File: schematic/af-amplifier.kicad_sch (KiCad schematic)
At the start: 34 parts, among them J2 AudioJack3, Q5 2N3904, U7 TDA2003, U8 ADE-1L

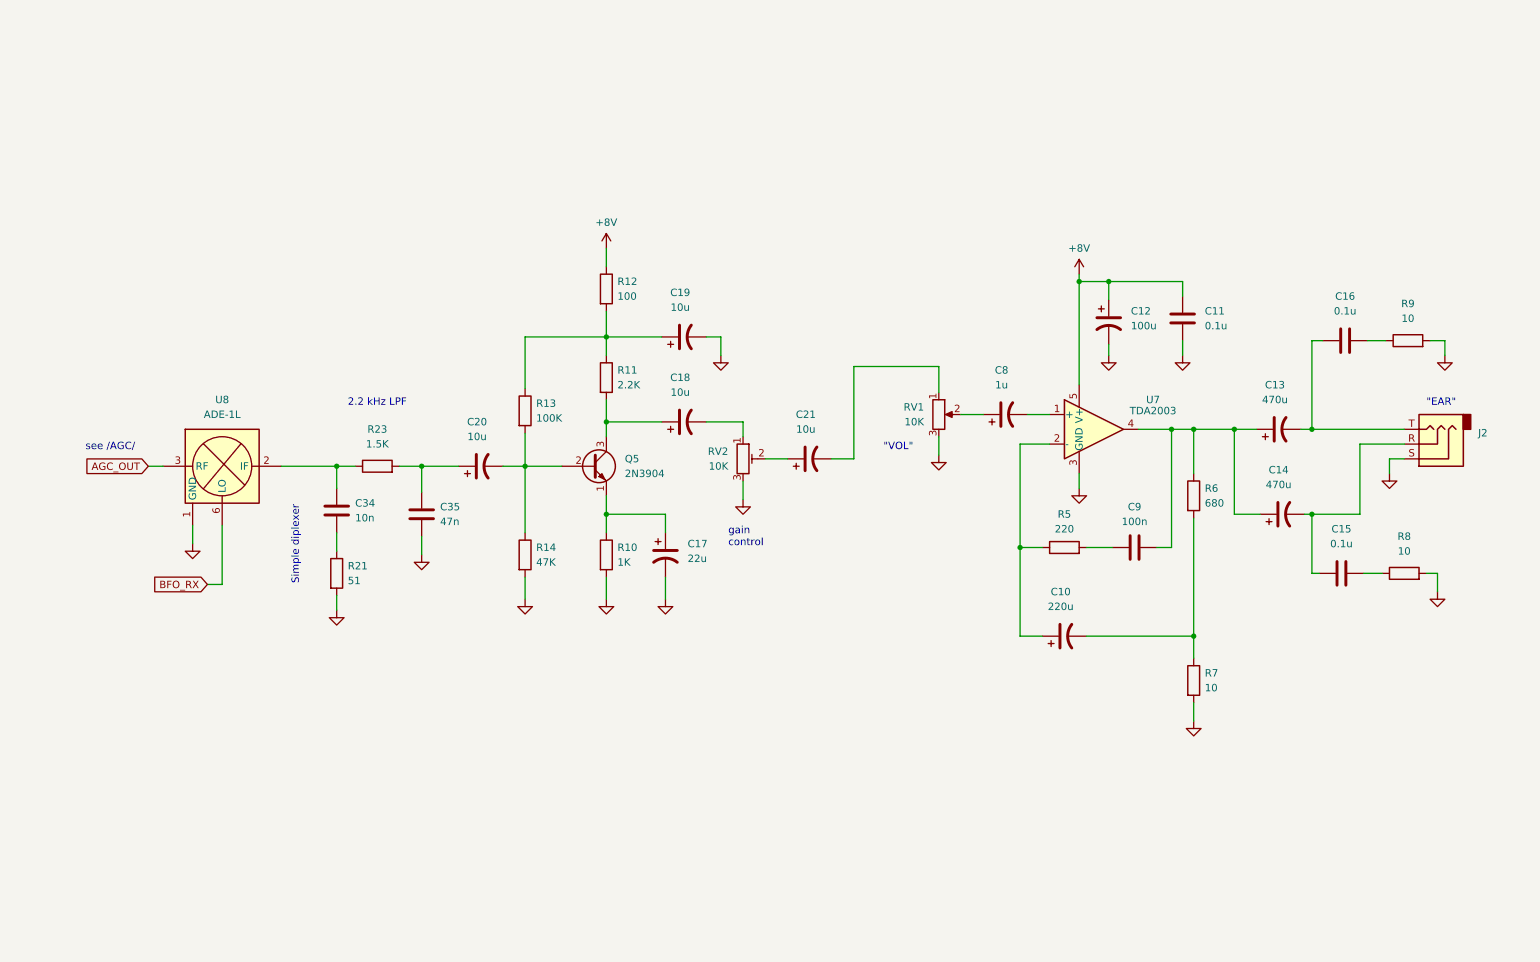
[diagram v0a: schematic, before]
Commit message: Schematic: add S-meter
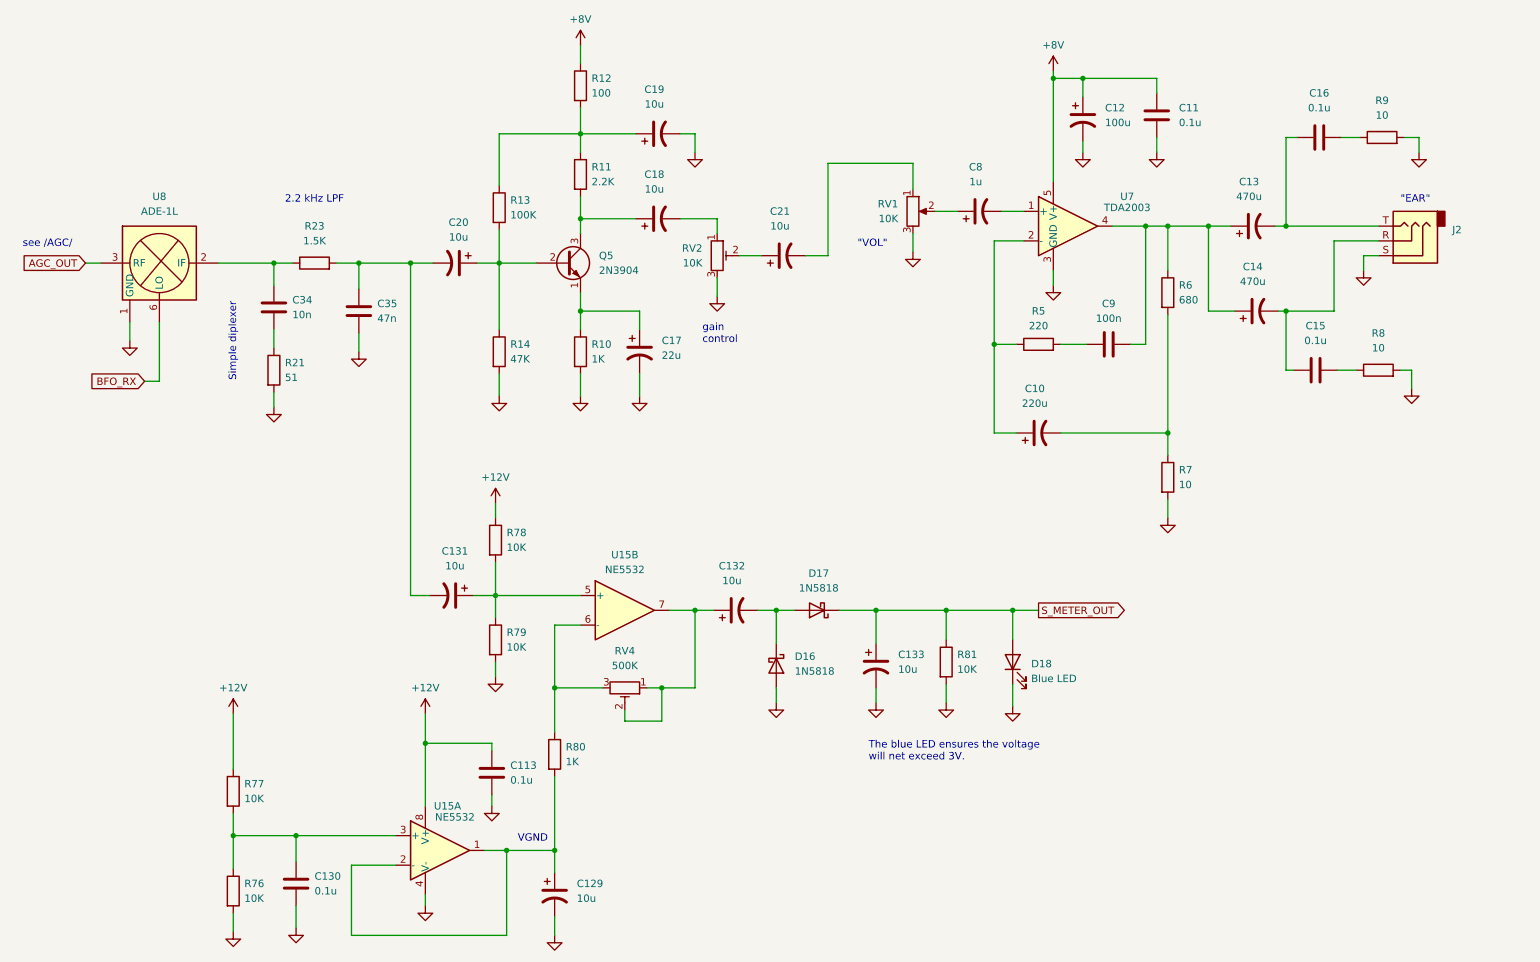
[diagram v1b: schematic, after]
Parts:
- added C113, C130: 0.1u, symbol Device:C
- added C129, C131, C132, C133: 10u, symbol Device:C_Polarized_US
- added D16, D17: 1N5818, Diode_THT:D_DO-41_SOD81_P10.16mm_Horizontal, symbol Diode:1N5818
- added D18: Blue LED, symbol Device:LED
- added R76, R77, R78, R79, R81: 10K, symbol Device:R
- added R80: 1K, symbol Device:R
- added RV4: 500K, symbol Device:R_Potentiometer_Trim
- added U15: NE5532, symbol Amplifier_Operational:NE5532
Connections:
- net GND: now also C113.2, C129.2, C130.2, C133.2, D16.2 (A), D18.1 (K), R76.2, R79.2, R81.2, U15.4 (V-)
- net at Q5.2 (B), R13.2, R14.1: now also C20.1; no longer C20.2
- net at C35.1, R23.2: now also C20.2, C131.2; no longer C20.1
- new net: C131.1, R78.2, R79.1, U15.5 (+)
- new net: C129.1, R80.2, U15.1, U15.2 (-)
- new net: C130.1, R76.1, R77.2, U15.3 (+)
- new net: C132.1, RV4.1, RV4.2, U15.7
- new net: C132.2, D16.1 (K), D17.2 (A)
- new net: R80.1, RV4.3, U15.6 (-)
- new net +12V: C113.1, R77.1, R78.1, U15.8 (V+)
- new net S_METER_OUT: C133.1, D17.1 (K), D18.2 (A), R81.1
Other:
- note added: "The blue LED ensures the voltage will net exceed 3V."
- note added: "VGND"
- moved on the sheet: C10, C11, C12, C13, C14, C15, C16, C17, C18, C19, C20, C21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

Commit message: Fix typo
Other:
- note added: "The blue LED ensures the voltage will not exceed 3V."
- note removed: "The blue LED ensures the voltage will net exceed 3V."
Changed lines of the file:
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@@
     (effects (font (size 1.27 1.27)) (justify left bottom))
   )
-  (text "The blue LED ensures the voltage\nwill net exceed 3V."
+  (text "The blue LED ensures the voltage\nwill not exceed 3V."
     (at 161.29 153.67 0)
     (effects (font (size 1.27 1.27)) (justify left bottom))

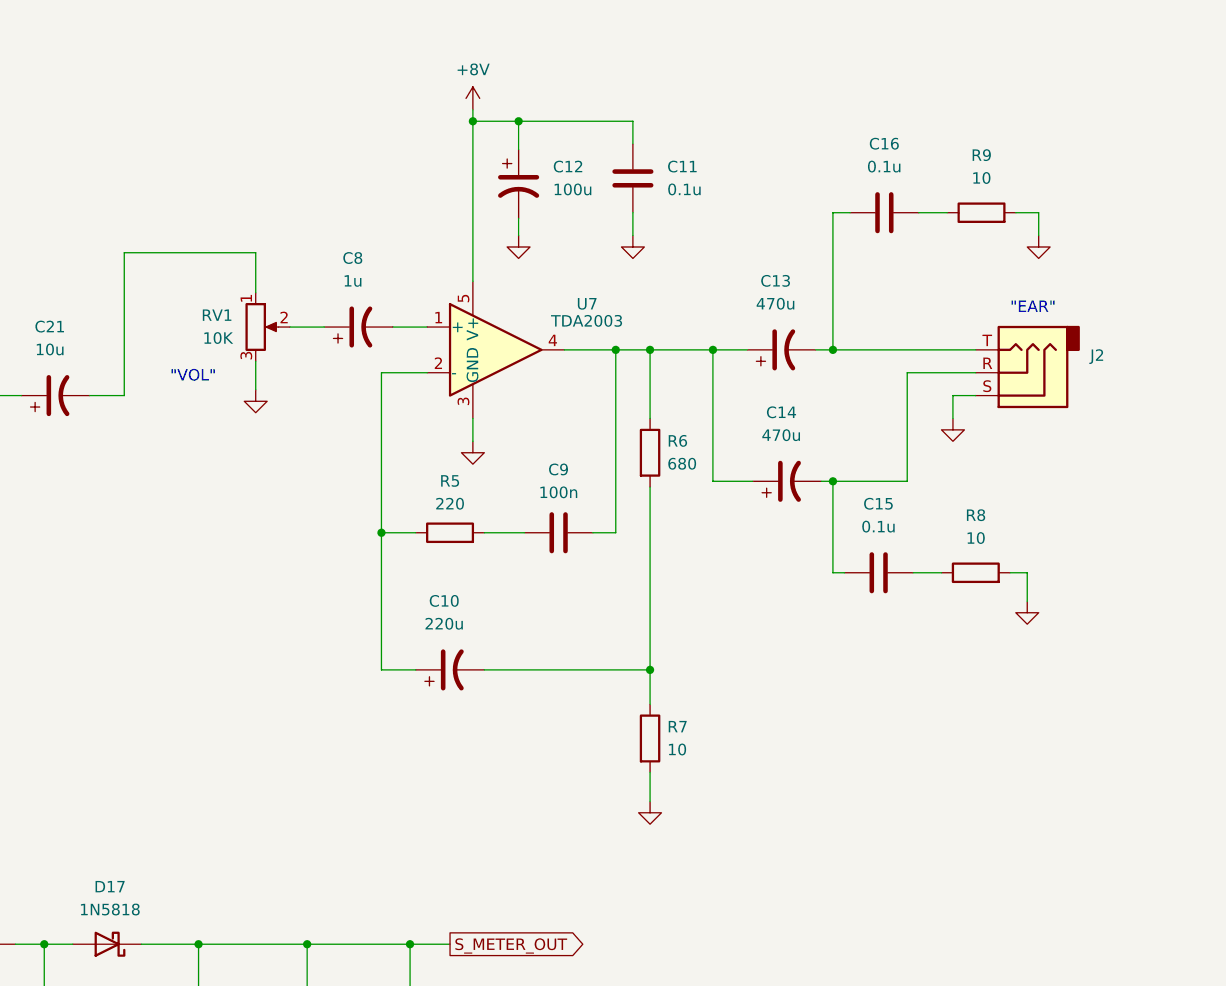
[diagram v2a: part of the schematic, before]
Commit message: Add CW tone generator + other changes
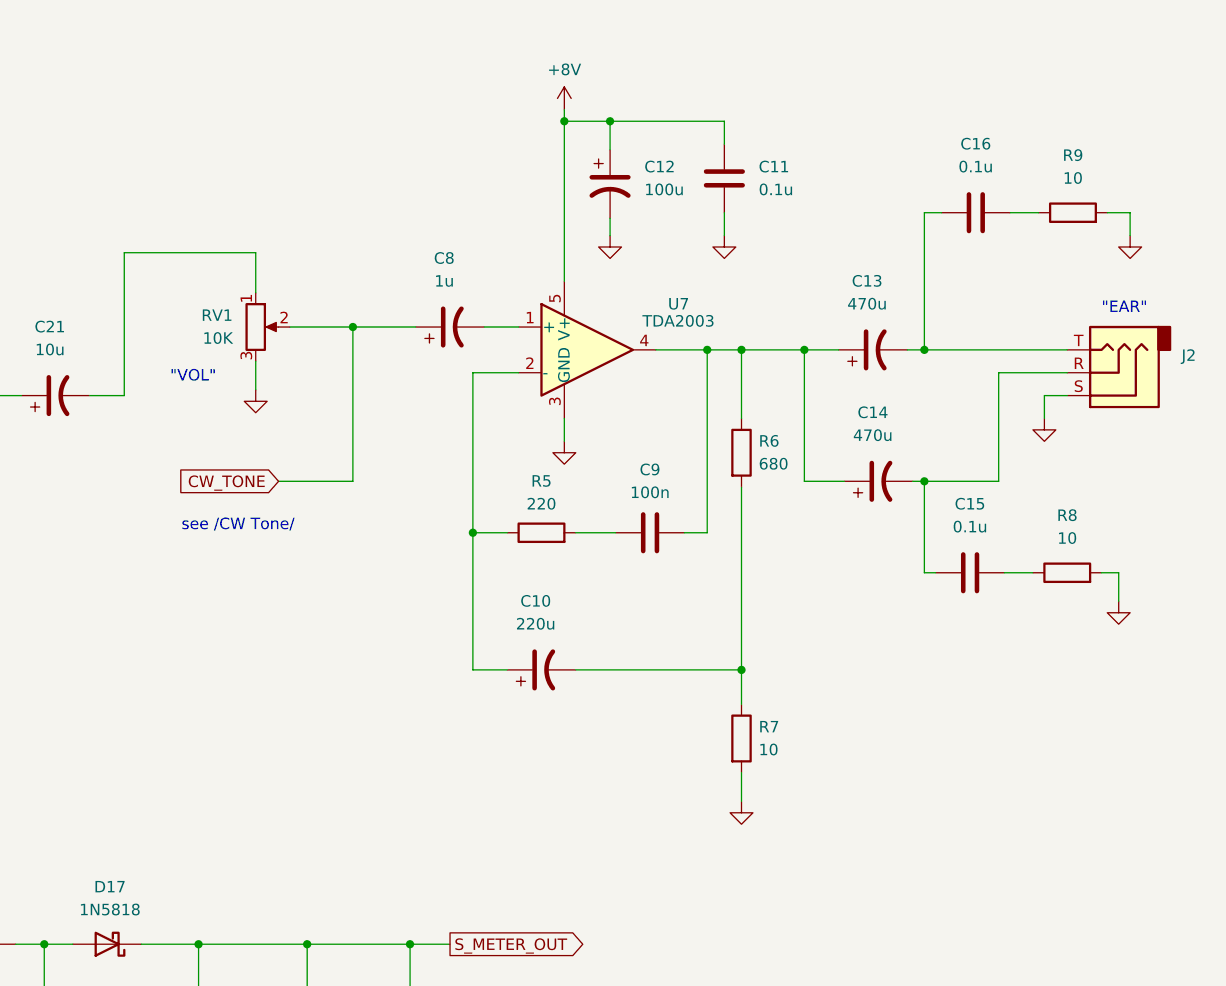
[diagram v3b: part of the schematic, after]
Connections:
- net CW_TONE: now reaches C8.1, RV1.2
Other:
- note added: "see /CW Tone/"
- moved on the sheet: C10, C11, C12, C13, C14, C15, C16, C8, C9, J2, R5, R6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

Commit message: Power S-meter from 8V
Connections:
- net +12V is gone; now on net +8V: C113.1, R77.1, R78.1, U15.8 (V+)

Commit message: Schematic: minor changes
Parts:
- U8: value ADE-1L -> ADE-6
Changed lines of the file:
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@@
       (effects (font (size 1.27 1.27)))
     )
-    (property "Value" "ADE-1L" (at 39.37 59.055 0)
+    (property "Value" "ADE-6" (at 39.37 59.055 0)
       (effects (font (size 1.27 1.27)))
     )

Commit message: Add 1.3K resistor before the volume control pot
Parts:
- added R101: 1.3K, symbol Device:R
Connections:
- net at C21.2: now also R101.1; no longer RV1.1
- new net: R101.2, RV1.1
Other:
- note added: "This resistor ensures that gain control of the driver has no effect on CW_TONE volume."
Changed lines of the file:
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@@
+    (stroke (width 0) (type default))
+  )
+  (wire (pts (xy 154.305 50.8) (xy 158.115 50.8))
     (stroke (width 0) (type default))
   )
@@
     (stroke (width 0) (type default))
   )
-  (wire (pts (xy 154.305 50.8) (xy 168.91 50.8))
-    (stroke (width 0) (type default))
-  )
   (wire (pts (xy 193.04 81.915) (xy 196.85 81.915))
     (stroke (width 0) (type default))
@@
   )
   (wire (pts (xy 107.315 140.97) (xy 107.315 130.175))
+    (stroke (width 0) (type default))
+  )
+  (wire (pts (xy 165.735 50.8) (xy 168.91 50.8))
     (stroke (width 0) (type default))
   )
@@
   )
   (text "see /AGC/" (at 15.875 65.405 0)
+    (effects (font (size 1.27 1.27)) (justify left bottom))
+  )
+  (text "This resistor ensures\nthat gain control\nof the driver has\nno effect on CW_TONE\nvolume."
+    (at 154.305 43.18 0)
     (effects (font (size 1.27 1.27)) (justify left bottom))
   )
@@
         )
       )
+    )
+  )
+  (symbol (lib_id "Device:R") (at 161.925 50.8 90) (unit 1)
+    (in_bom yes) (on_board yes) (dnp no) (fields_autoplaced)
+    (property "Reference" "R101" (at 161.925 45.085 90)
+      (effects (font (size 1.27 1.27)))
+    )
+    (property "Value" "1.3K" (at 161.925 47.625 90)
+      (effects (font (size 1.27 1.27)))
+    )
+    (property "Footprint" "" (at 161.925 52.578 90)
+      (effects (font (size 1.27 1.27)) hide)
+    )
+    (property "Datasheet" "~" (at 161.925 50.8 0)
+      (effects (font (size 1.27 1.27)) hide)
+    )
+    (pin "1")
+    (pin "2")
+    (instances
+      (project "hbr-mk2"
+        (path "/700c9878-4ed7-49d5-a273-77cf9d92989d/56e6206b-9eaf-48e3-8e65-5aed78d22a1d"
+          (reference "R101") (unit 1)
+        )
+      )
